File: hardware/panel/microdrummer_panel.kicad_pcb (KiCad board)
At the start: 2 copper layers, 20 x 128.5 mm, 10 parts

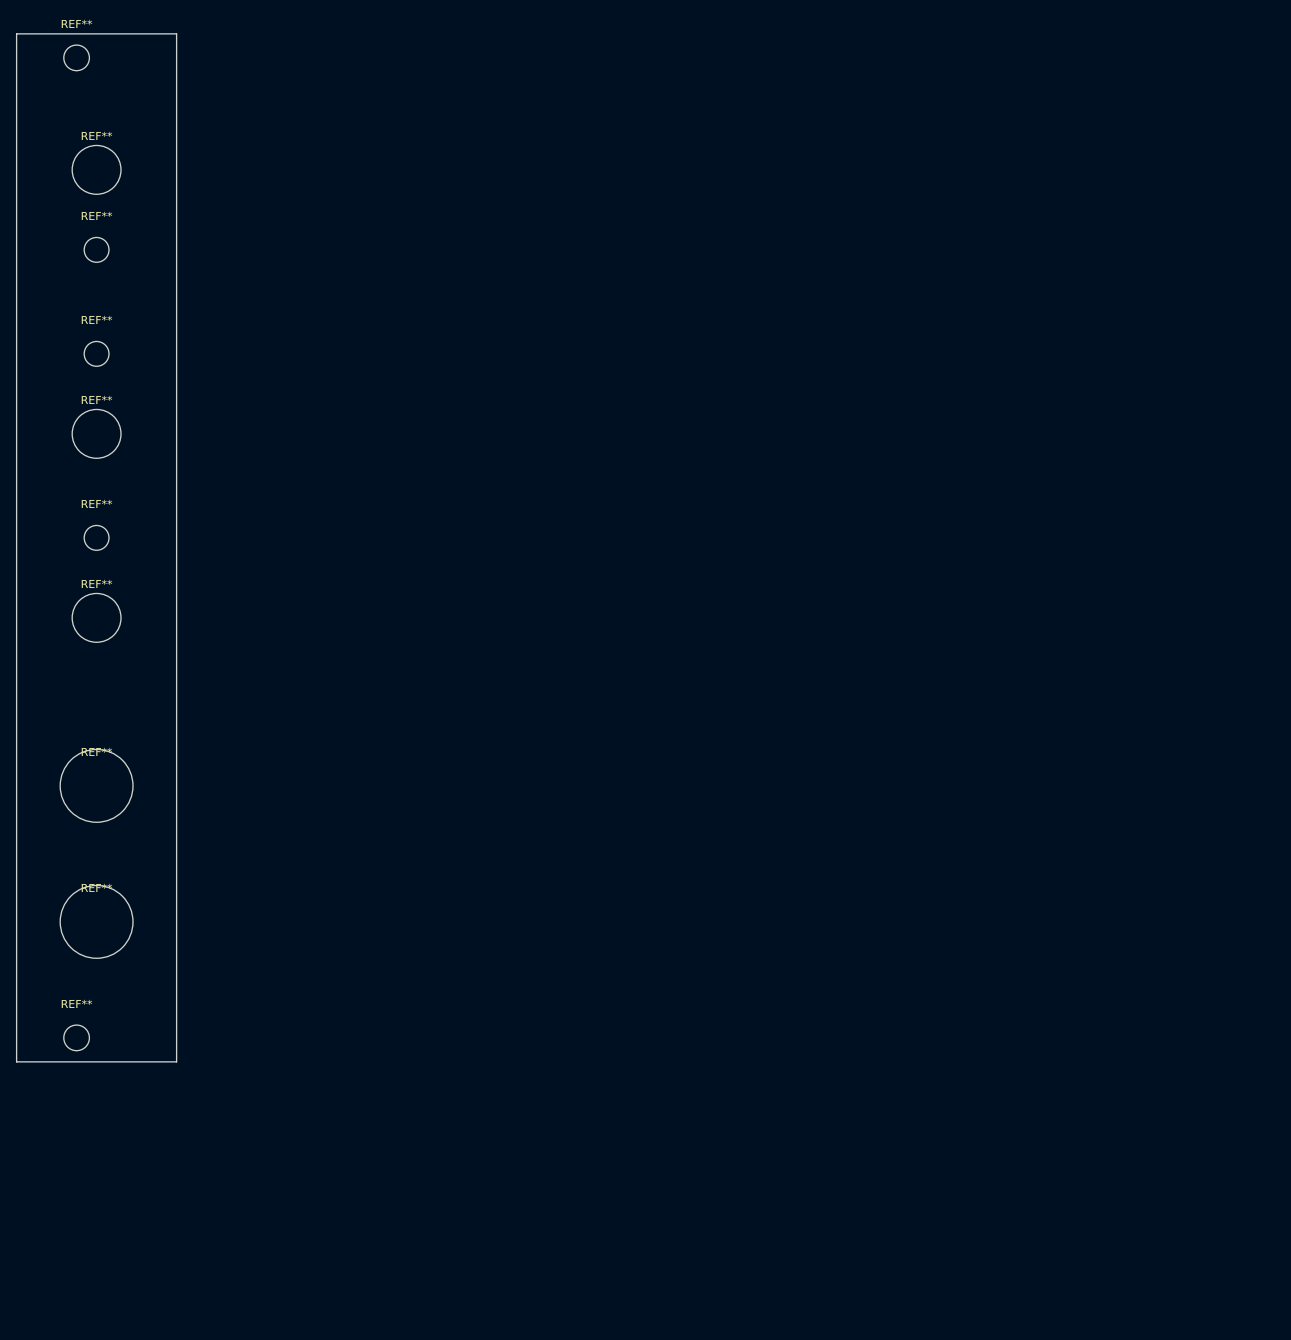
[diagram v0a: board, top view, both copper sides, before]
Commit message: layout updates, and moved pins around for 1-layer routing
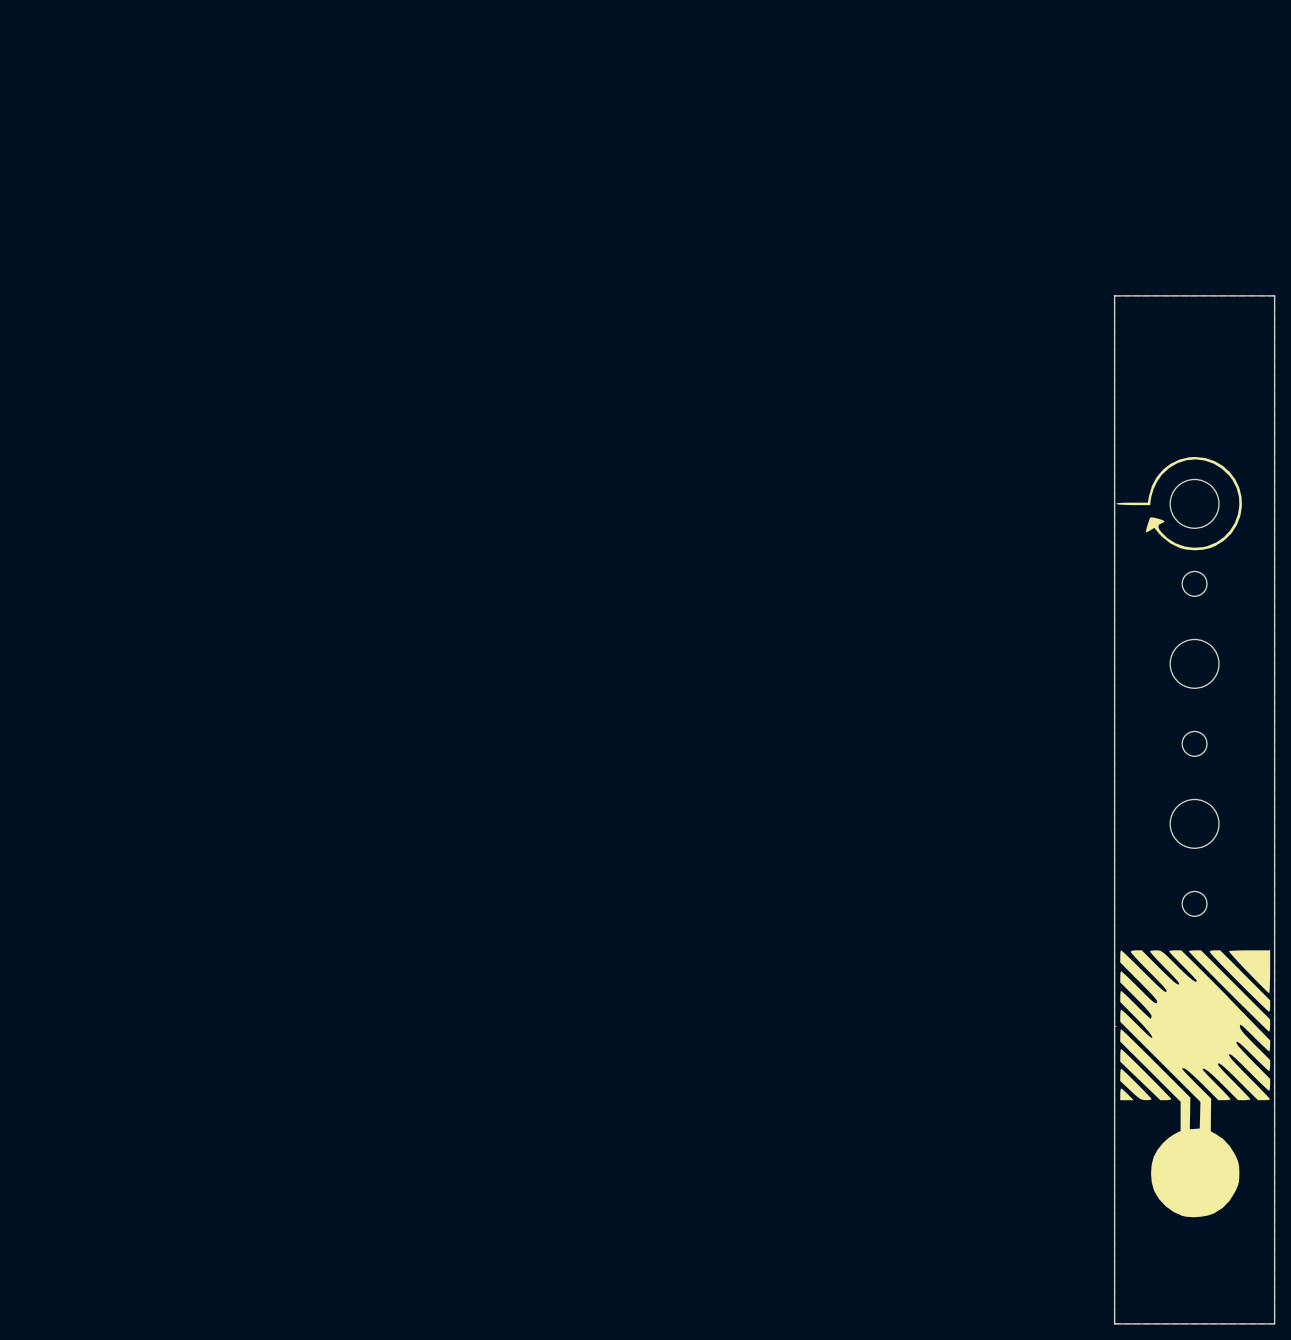
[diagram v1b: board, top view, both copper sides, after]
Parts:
- removed the REF** at (7.50, 3.00)
- removed the REF** at (7.50, 125.5)
- added G***: LOGO, drill_holes:sig_in, F.Cu at (147.2, 58.8)
- added G***: LOGO, drill_holes:btns, F.Cu at (147.2, 131.2)
- added G***: LOGO, drill_holes:cp_half_inch, F.Cu at (147.2, 45.2)
- added REF**: M3_Slot, drill_holes:M3_Slot, F.Cu at (144.8, 158.2)
- added REF**: M3_Slot, drill_holes:M3_Slot, F.Cu at (144.8, 35.8)
- moved REF** 145.7 mm to (147.2, 88.8)
- moved REF** 144.7 mm to (147.2, 108.8)
- moved REF** 143.5 mm to (147.2, 58.8)
- moved REF** 143.5 mm to (147.2, 68.8)
- moved REF** 140.8 mm to (147.2, 142.5)
- moved REF** 140.5 mm to (147.2, 124.0)
- moved REF** 140.2 mm to (147.2, 78.8)
- moved REF** 139.6 mm to (147.2, 98.8)
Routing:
- added copper zone on F.Cu, net (none)
